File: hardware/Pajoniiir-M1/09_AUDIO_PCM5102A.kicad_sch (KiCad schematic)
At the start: 23 parts, among them U5 PCM5102APWR

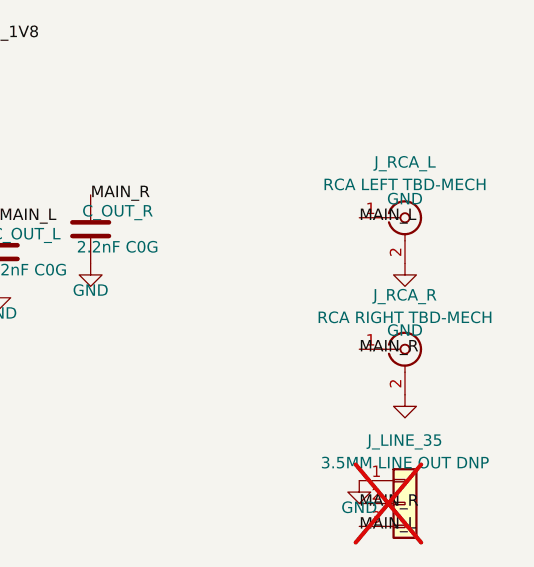
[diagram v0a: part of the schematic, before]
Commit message: ci: capture KiCad 9 symbols and repair PGTH junction
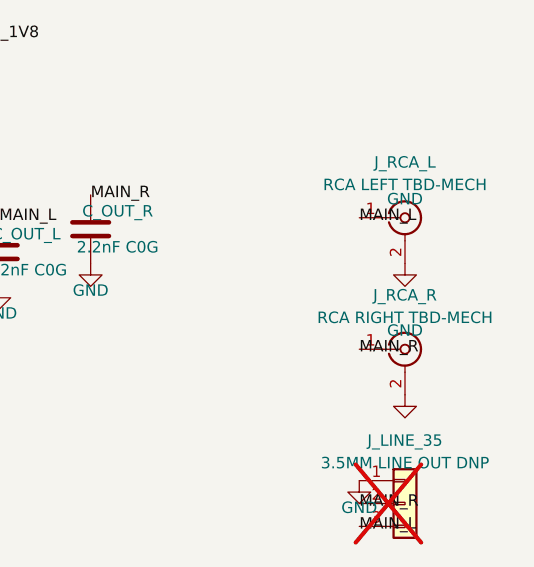
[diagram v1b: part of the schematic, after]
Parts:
- J_RCA_L, J_RCA_R: symbol Pajoniiir-M1:Conn_Coaxial_M1 -> Connector:Conn_Coaxial
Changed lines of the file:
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@@
   )
   (symbol
-    (lib_id "Pajoniiir-M1:Conn_Coaxial_M1") (at 224.79 90.17 0) (unit 1)
+    (lib_id "Connector:Conn_Coaxial") (at 224.79 90.17 0) (unit 1)
     (exclude_from_sim no) (in_bom yes) (on_board yes) (dnp no)
     (property "Reference" "J_RCA_L" (at 224.79 84.01 0) (effects (font (size 1.27 1.27))))
@@
   )
   (symbol
-    (lib_id "Pajoniiir-M1:Conn_Coaxial_M1") (at 224.79 104.775 0) (unit 1)
+    (lib_id "Connector:Conn_Coaxial") (at 224.79 104.775 0) (unit 1)
     (exclude_from_sim no) (in_bom yes) (on_board yes) (dnp no)
     (property "Reference" "J_RCA_R" (at 224.79 98.775 0) (effects (font (size 1.27 1.27))))

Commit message: hardware: pin Rev-A symbols to local library copies
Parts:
- J_RCA_L, J_RCA_R: symbol Connector:Conn_Coaxial -> Pajoniiir-M1:Conn_Coaxial_M1
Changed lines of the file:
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@@
   )
   (symbol
-    (lib_id "Connector:Conn_Coaxial") (at 224.79 90.17 0) (unit 1)
+    (lib_id "Pajoniiir-M1:Conn_Coaxial_M1") (at 224.79 90.17 0) (unit 1)
     (exclude_from_sim no) (in_bom yes) (on_board yes) (dnp no)
     (property "Reference" "J_RCA_L" (at 224.79 84.01 0) (effects (font (size 1.27 1.27))))
@@
   )
   (symbol
-    (lib_id "Connector:Conn_Coaxial") (at 224.79 104.775 0) (unit 1)
+    (lib_id "Pajoniiir-M1:Conn_Coaxial_M1") (at 224.79 104.775 0) (unit 1)
     (exclude_from_sim no) (in_bom yes) (on_board yes) (dnp no)
     (property "Reference" "J_RCA_R" (at 224.79 98.775 0) (effects (font (size 1.27 1.27))))
